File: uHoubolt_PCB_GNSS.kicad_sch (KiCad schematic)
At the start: 92 parts, among them J1 Power In, J10 CAN1, J11 CAN1, J2 Debug, J3 Debug, J4 CAN1, J5 CAN1, J6 CAN1, J7 CAN1, J8 CAN1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

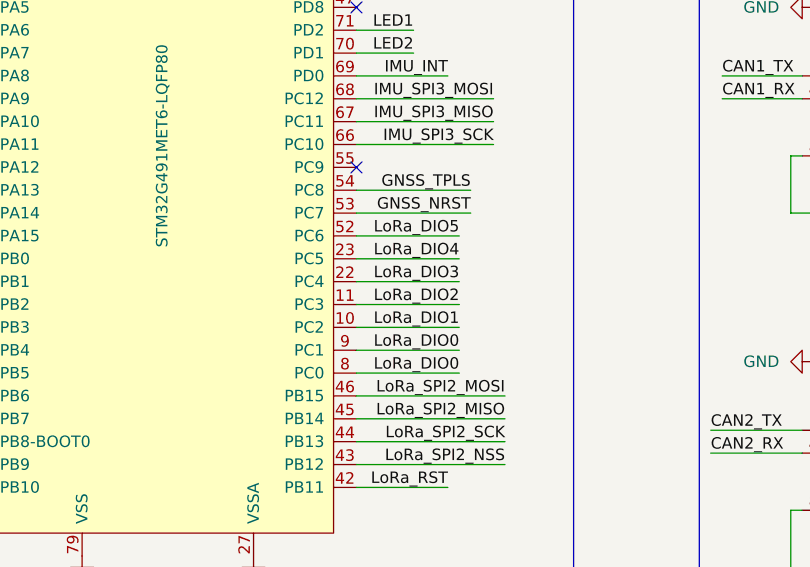
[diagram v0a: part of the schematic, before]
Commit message: Fix LoRa DIO missconnection to STM32
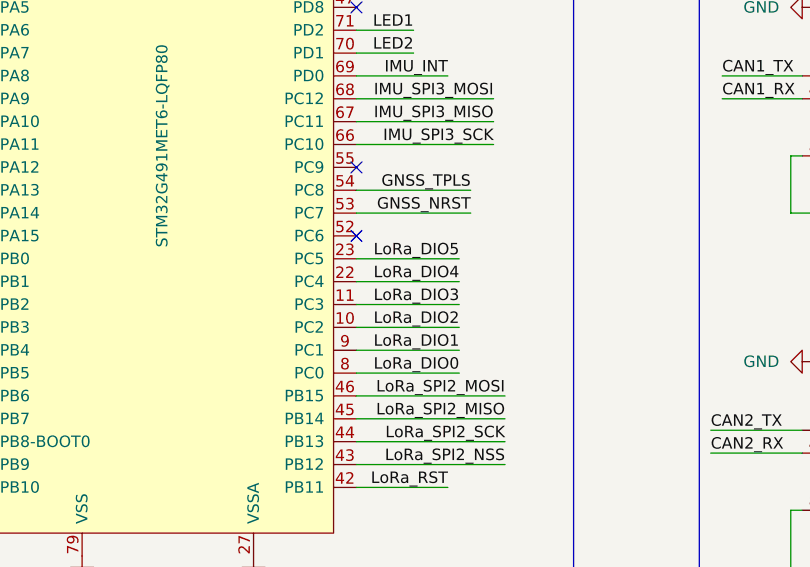
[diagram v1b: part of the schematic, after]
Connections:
- net LoRa_DIO0: no longer U2.9 (PC1)
- net LoRa_DIO1: now also U2.9 (PC1); no longer U2.10 (PC2)
- net LoRa_DIO2: now also U2.10 (PC2); no longer U2.11 (PC3)
- net LoRa_DIO3: now also U2.11 (PC3); no longer U2.22 (PC4)
- net LoRa_DIO4: now also U2.22 (PC4); no longer U2.23 (PC5)
- net LoRa_DIO5: now also U2.23 (PC5); no longer U2.52 (PC6)
- no-connect marks 26 -> 27
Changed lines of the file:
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@@
   (no_connect (at 133.35 176.53))
   (no_connect (at 133.35 166.37))
+  (no_connect (at 133.35 204.47))
   (no_connect (at 222.25 72.39))
   (no_connect (at 262.89 137.16))
@@
     (stroke (width 0) (type default) (color 0 0 0 0))
   )
-  (wire (pts (xy 133.35 204.47) (xy 144.78 204.47))
-    (stroke (width 0) (type default) (color 0 0 0 0))
-  )
   (wire (pts (xy 292.1 57.15) (xy 292.1 55.88))
     (stroke (width 0) (type default) (color 0 0 0 0))
@@
     (effects (font (size 1.27 1.27)) (justify left bottom))
   )
-  (label "LoRa_DIO4" (at 144.78 207.01 180)
+  (label "LoRa_DIO5" (at 144.78 207.01 180)
     (effects (font (size 1.27 1.27)) (justify right bottom))
   )
@@
     (effects (font (size 1.27 1.27)) (justify left bottom))
   )
-  (label "LoRa_DIO2" (at 144.78 212.09 180)
+  (label "LoRa_DIO3" (at 144.78 212.09 180)
     (effects (font (size 1.27 1.27)) (justify right bottom))
   )
@@
     (effects (font (size 1.27 1.27)) (justify right bottom))
   )
-  (label "LoRa_DIO1" (at 144.78 214.63 180)
+  (label "LoRa_DIO2" (at 144.78 214.63 180)
     (effects (font (size 1.27 1.27)) (justify right bottom))
   )
@@
     (effects (font (size 1.27 1.27)) (justify left bottom))
   )
-  (label "LoRa_DIO5" (at 144.78 204.47 180)
-    (effects (font (size 1.27 1.27)) (justify right bottom))
-  )
   (label "LoRa_DIO5" (at 342.9 156.21 180)
     (effects (font (size 1.27 1.27)) (justify right bottom))
@@
     (effects (font (size 1.27 1.27)) (justify left bottom))
   )
-  (label "LoRa_DIO3" (at 144.78 209.55 180)
+  (label "LoRa_DIO4" (at 144.78 209.55 180)
     (effects (font (size 1.27 1.27)) (justify right bottom))
   )
@@
     (effects (font (size 1.27 1.27)) (justify right bottom))
   )
-  (label "LoRa_DIO0" (at 144.78 217.17 180)
-    (effects (font (size 1.27 1.27)) (justify right bottom))
-  )
+  (label "LoRa_DIO1" (at 144.78 217.17 180)
+    (effects (font (size 1.27 1.27)) (justify right bottom))
+  )

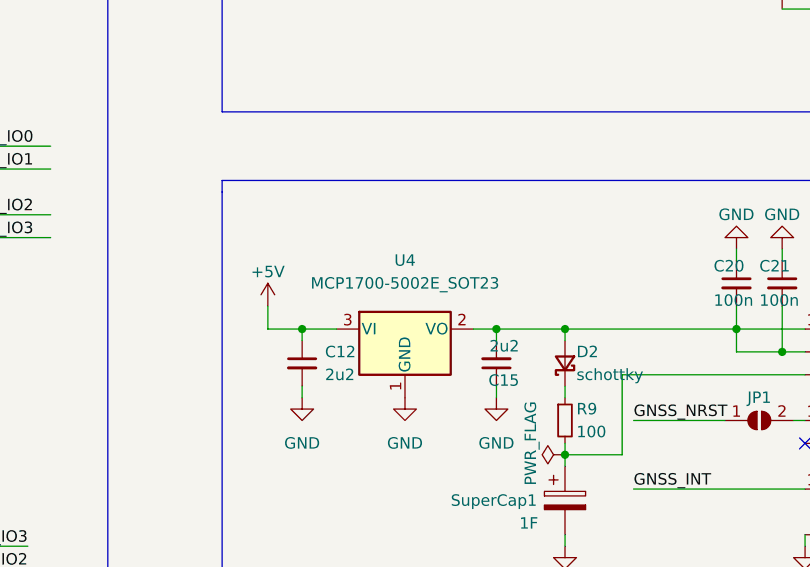
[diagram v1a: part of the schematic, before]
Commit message: Fix false LDO for GNSS --> +3V3
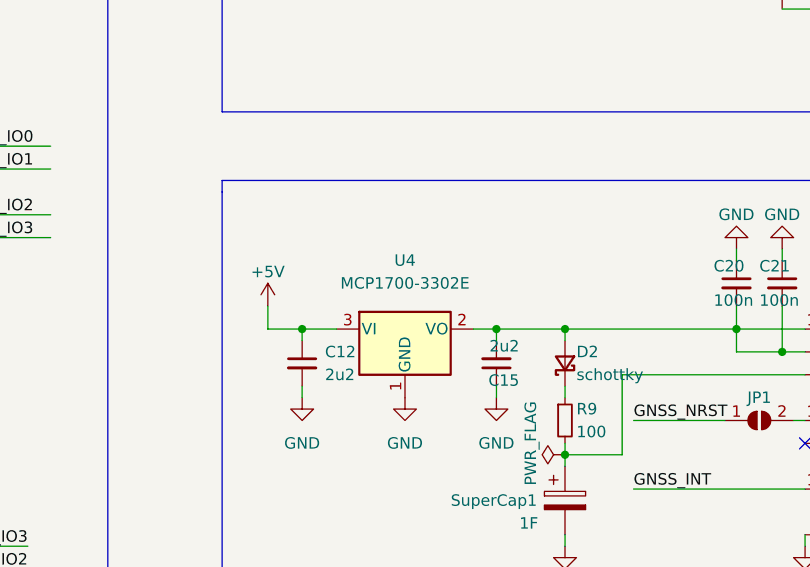
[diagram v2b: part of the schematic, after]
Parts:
- removed U4: MCP1700-5002E_SOT23, Package_TO_SOT_SMD:SOT-23, symbol Regulator_Linear:MCP1700-5002E_SOT23
- added U4: MCP1700-3302E, Package_TO_SOT_SMD:SOT-23, symbol Regulator_Linear:MCP1700-3302E_SOT23
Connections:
- net +5V: now also U4.3 (VI)
- net GND: now also U4.1 (GND)
- net at C15.2, C20.2, C21.2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: now also U4.2 (VO)
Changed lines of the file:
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@@
     (pin "4")
+  )
+  (symbol (lib_id "Regulator_Linear:MCP1700-3302E_SOT23") (at 190.5 127 0) (unit 1)
+    (in_bom yes) (on_board yes) (fields_autoplaced)
+    (property "Reference" "U4" (id 0) (at 190.5 119.38 0))
+    (property "Value" "MCP1700-3302E" (id 1) (at 190.5 121.92 0))
+    (property "Footprint" "Package_TO_SOT_SMD:SOT-23" (id 2) (at 190.5 121.285 0)
+      (effects (font (size 1.27 1.27)) hide)
+    )
+    (property "Datasheet" "http://ww1.microchip.com/downloads/en/DeviceDoc/20001826D.pdf" (id 3) (at 190.5 127 0)
+      (effects (font (size 1.27 1.27)) hide)
+    )
+    (pin "1")
+    (pin "2")
+    (pin "3")
   )
   (symbol (lib_id "power:GND") (at 236.22 199.39 0) (mirror y) (unit 1)
@@
     (pin "1")
   )
-  (symbol (lib_id "Regulator_Linear:MCP1700-5002E_SOT23") (at 190.5 127 0) (unit 1)
-    (in_bom yes) (on_board yes) (fields_autoplaced)
-    (property "Reference" "U4" (id 0) (at 190.5 119.38 0))
-    (property "Value" "MCP1700-5002E_SOT23" (id 1) (at 190.5 121.92 0))
-    (property "Footprint" "Package_TO_SOT_SMD:SOT-23" (id 2) (at 190.5 121.285 0)
-      (effects (font (size 1.27 1.27)) hide)
-    )
-    (property "Datasheet" "http://ww1.microchip.com/downloads/en/DeviceDoc/20001826D.pdf" (id 3) (at 190.5 127 0)
-      (effects (font (size 1.27 1.27)) hide)
-    )
-    (pin "1")
-    (pin "2")
-    (pin "3")
-  )
   (symbol (lib_id "power:+5V") (at 321.31 118.11 0) (unit 1)
     (in_bom yes) (on_board yes)
@@
       (reference "U3") (unit 1) (value "W25Q256JV") (footprint "")
     )
-    (path "/e4224aa3-ca8b-41fd-9f47-da89c432a4c3"
-      (reference "U4") (unit 1) (value "MCP1700-5002E_SOT23") (footprint "Package_TO_SOT_SMD:SOT-23")
+    (path "/213d10bd-6da1-43cd-94f6-1926533eb049"
+      (reference "U4") (unit 1) (value "MCP1700-3302E") (footprint "Package_TO_SOT_SMD:SOT-23")
     )
     (path "/37b30c26-45de-42b5-935d-15044d028df3"

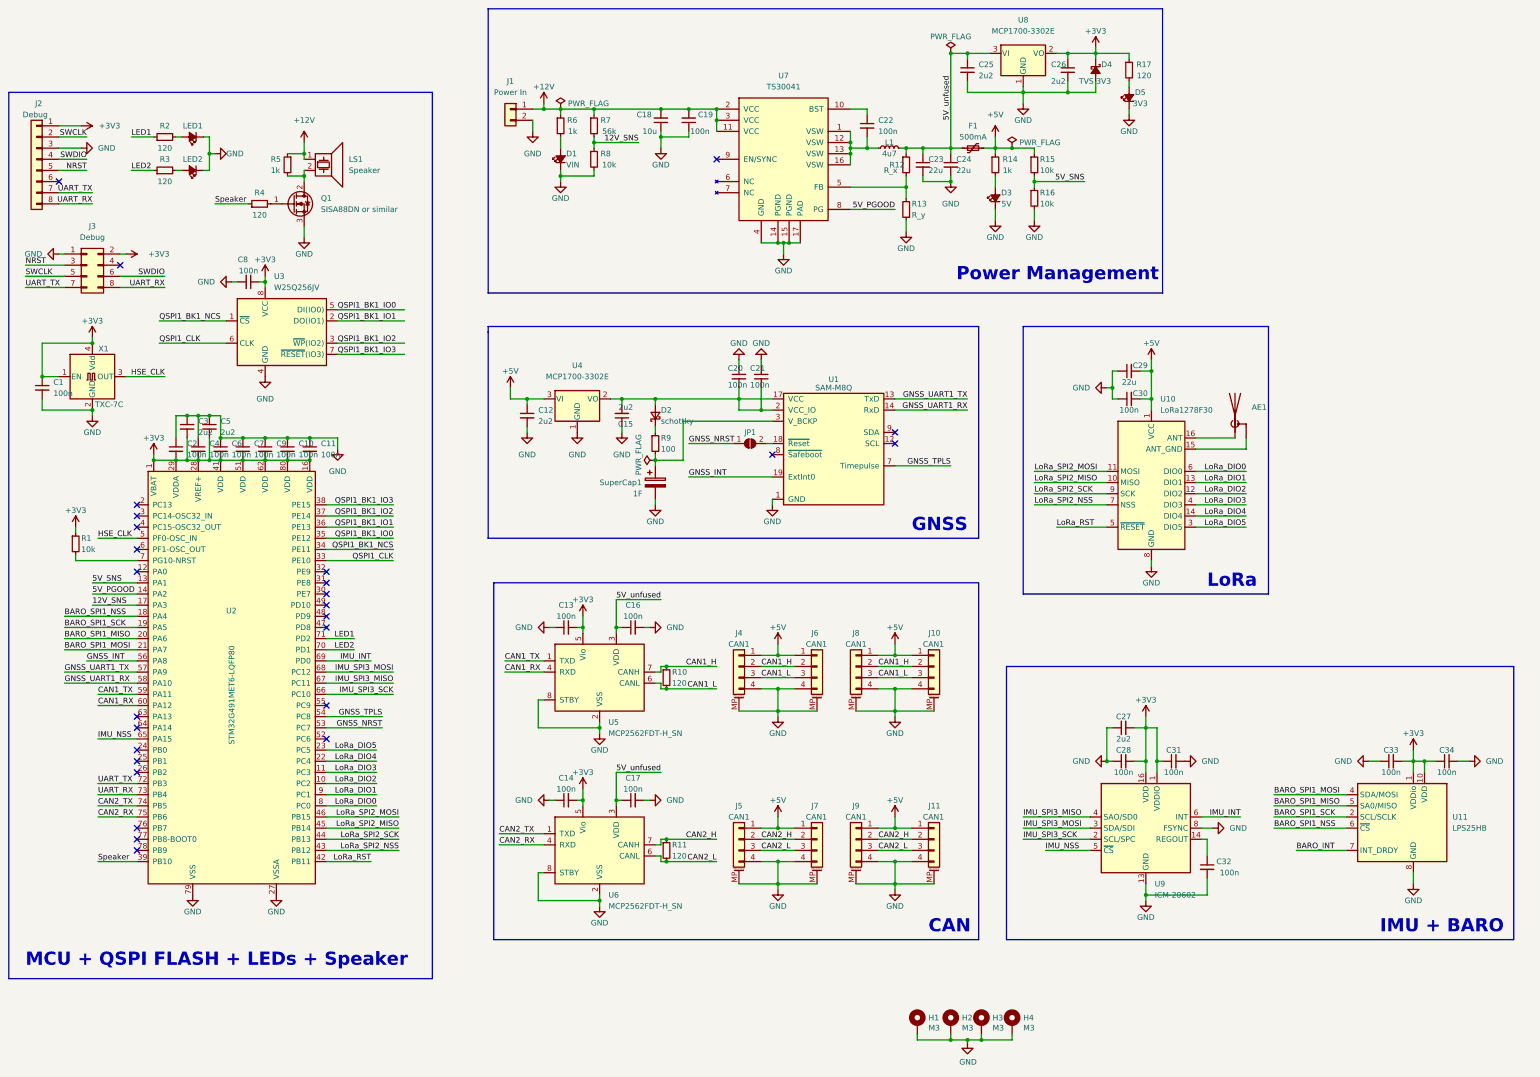
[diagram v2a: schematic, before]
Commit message: Update footprints and fixed minor naming fails.
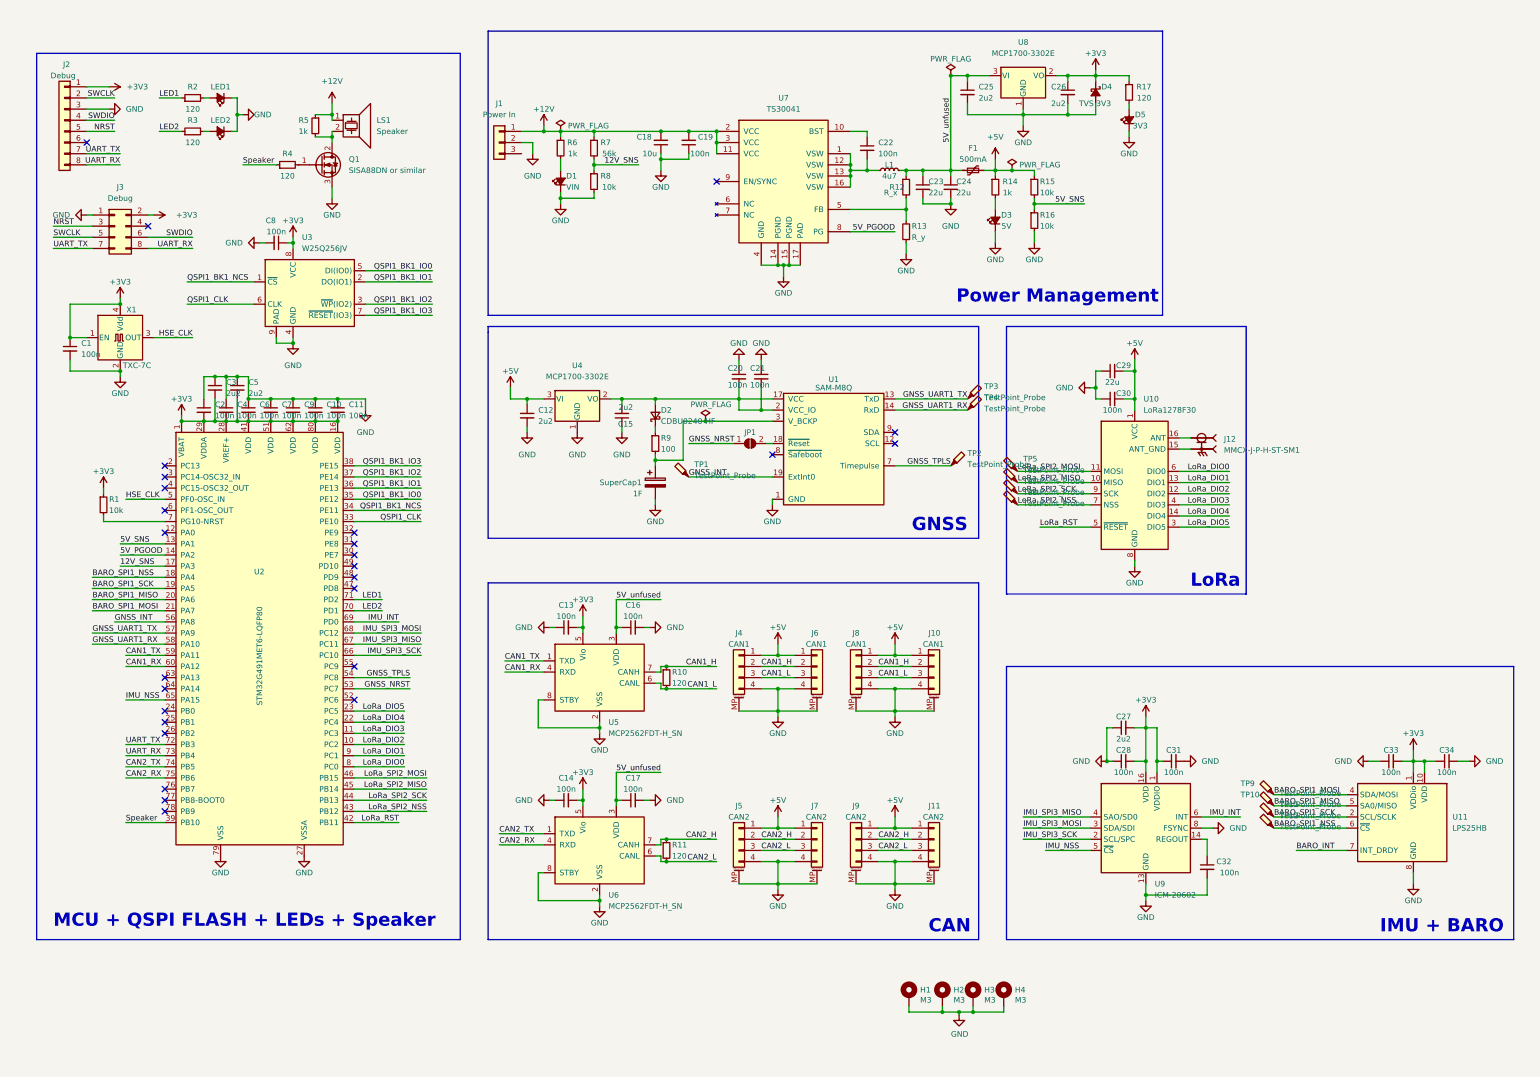
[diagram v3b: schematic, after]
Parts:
- removed AE1: Antenna_Shield, symbol Device:Antenna_Shield
- removed J1: Power In, symbol Connector_Generic:Conn_01x02
- removed U10: LoRa1278F30, symbol add_components:LoRa1278F30
- added J1: Power In, TXV_Library_Footprints:Molex_MegaFit_1x03_Vertical, symbol Connector_Generic:Conn_01x03
- added J12: MMCX-J-P-H-ST-SM1, TXV_Library_Footprints:SAMTEC_MMCX-J-P-H-ST-SM1, symbol add_components:MMCX-J-P-H-ST-SM1
- added TP1, TP10, TP11, TP12, TP2, TP3, TP4, TP5, TP6, TP7, TP8, TP9: TestPoint_Probe, TestPoint:TestPoint_Pad_D1.0mm, symbol Connector:TestPoint_Probe
- added U10: LoRa1278F30, symbol TXV_Library_Symbols:LoRa1278F30
- D2: value schottky -> CDBU0240-HF; footprint (none) -> Diode_SMD:D_SOD-323F
- D4: footprint (none) -> TXV_Library_Footprints:SOD882D
- F1: footprint Fuse_1206_3216Metric -> Fuse:Fuse_0603_1608Metric
- J10, J4, J6, J8: footprint (none) -> Connector_JST:JST_GH_BM04B-GHS-TBT_1x04-1MP_P1.25mm_Vertical
- J11, J5, J7, J9: value CAN1 -> CAN2; footprint (none) -> Connector_JST:JST_GH_BM04B-GHS-TBT_1x04-1MP_P1.25mm_Vertical
- J2: footprint Connector_PinHeader_1.27mm:PinHeader_2x04_P1.27mm_Vertical_SMD -> Connector_PinHeader_2.54mm:PinHeader_1x08_P2.54mm_Vertical_SMD_Pin1Left
- J3: footprint (none) -> Connector_PinHeader_1.27mm:PinHeader_2x04_P1.27mm_Vertical_SMD
- JP1: footprint (none) -> Jumper:SolderJumper-2_P1.3mm_Open_Pad1.0x1.5mm
- L1: footprint (none) -> TXV_Library_Footprints:SRN4018TA-4R7M
- LED1, LED2: footprint (none) -> LED_SMD:LED_0603_1608Metric
- LS1: footprint (none) -> TXV_Library_Footprints:Piezo_Buzzer
- Q1: footprint (none) -> TXV_Library_Footprints:PowerPAK_1212-8
- SuperCap1: footprint (none) -> Capacitor_SMD:CP_Elec_10x10.5
- U3: footprint (none) -> TXV_Library_Footprints:WSON-8-8x6mm
- U7: footprint Housings_DFN_QFN:QFN-16-1EP_3x3mm_Pitch0.5mm -> Package_DFN_QFN:QFN-16-1EP_3x3mm_P0.5mm_EP1.75x1.75mm_ThermalVias
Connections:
- net +12V: now also J1.1 (Pin_1)
- net +5V: now also U10.1 (VCC)
- net BARO_SPI1_MISO: now also TP10.1
- net BARO_SPI1_MOSI: now also TP9.1
- net BARO_SPI1_NSS: now also TP12.1
- net BARO_SPI1_SCK: now also TP11.1
- net GND: now also U3.9 (PAD), J1.2 (Pin_2), U10.8 (GND)
- net GNSS_INT: now also TP1.1
- net GNSS_TPLS: now also TP2.1
- net GNSS_UART1_RX: now also TP4.1
- net GNSS_UART1_TX: now also TP3.1
- net LoRa_DIO0: now also U10.6 (DIO0)
- net LoRa_DIO1: now also U10.13 (DIO1)
- net LoRa_DIO2: now also U10.12 (DIO2)
- net LoRa_DIO3: now also U10.4 (DIO3)
- net LoRa_DIO4: now also U10.14 (DIO4)
- net LoRa_DIO5: now also U10.3 (DIO5)
- net LoRa_RST: now also U10.5 (~{RESET})
- net LoRa_SPI2_MISO: now also TP6.1, U10.10 (MISO)
- net LoRa_SPI2_MOSI: now also TP5.1, U10.11 (MOSI)
- net LoRa_SPI2_NSS: now also TP8.1, U10.7 (NSS)
- net LoRa_SPI2_SCK: now also TP7.1, U10.9 (SCK)
- new net: J12.S1, J12.S2, J12.S3, J12.S4, U10.15 (ANT_GND)
- new net: J12.1, U10.16 (ANT)
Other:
- moved on the sheet: C1, C10, C11, C18, C19, C2, C22, C23, C24, C25, C26, C29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
